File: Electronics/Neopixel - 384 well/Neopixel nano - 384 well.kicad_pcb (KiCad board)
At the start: 2 copper layers, 121.5 x 83 mm, 777 parts, among them J1 USB_B, J2 Conn_01x03_Male, U1 SAMD21_MOD

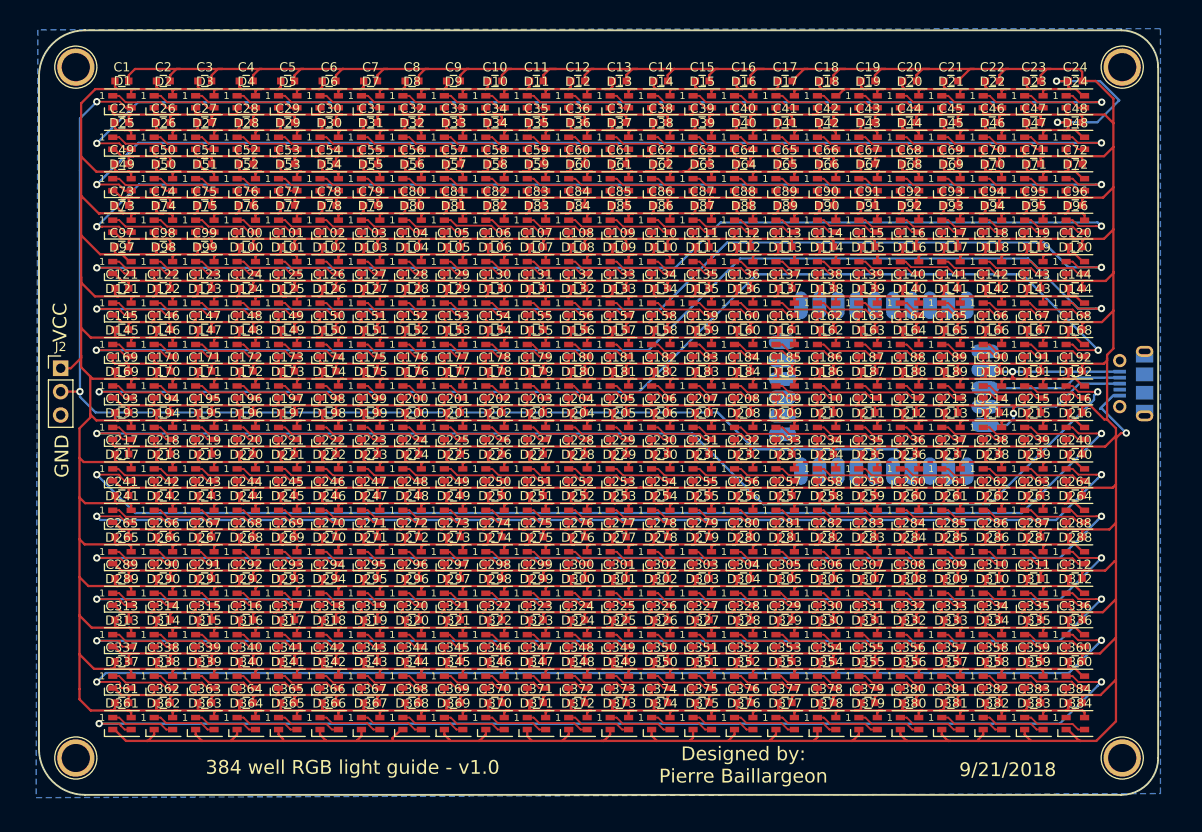
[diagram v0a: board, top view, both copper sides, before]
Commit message: Updated to v1.1
Updated to v1.1. Changes:
- Removed HCC module footprint from back to simplify design
- Added copper pour to front of PCB for +5V
- Added fiducuals for pick and place automation
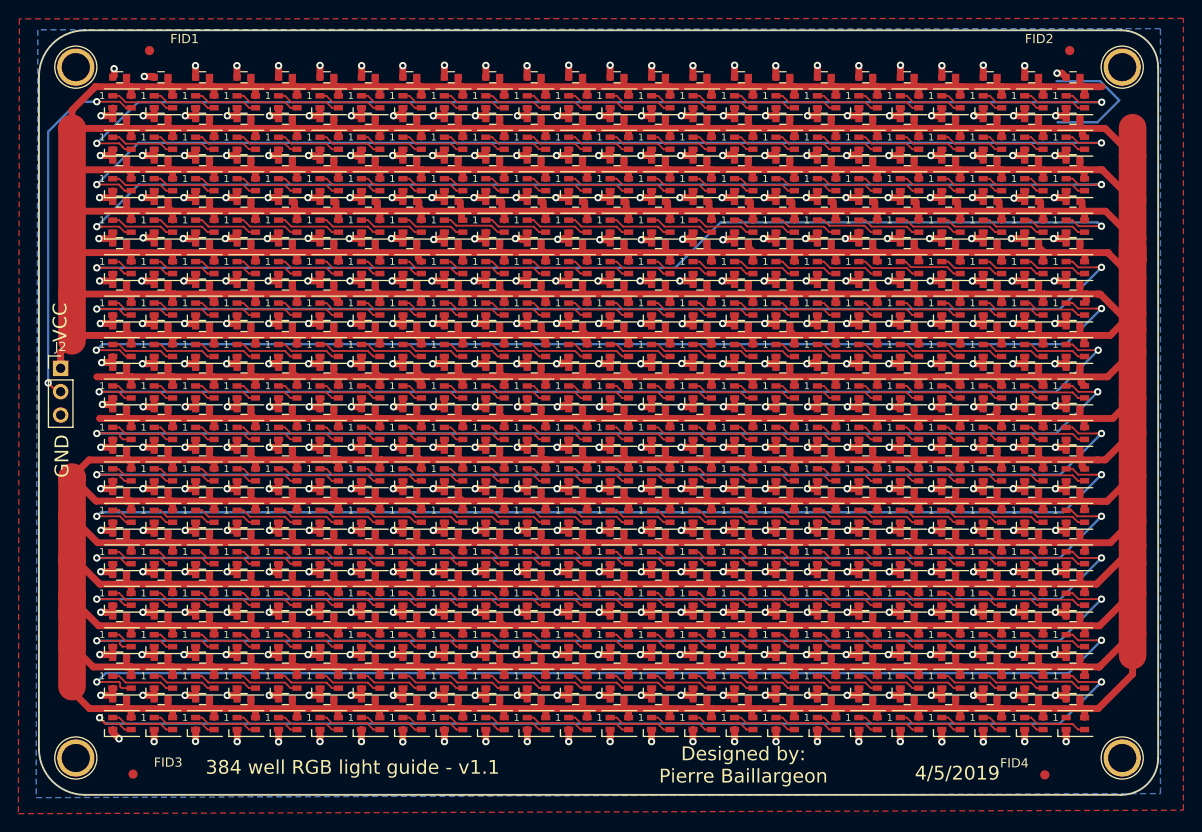
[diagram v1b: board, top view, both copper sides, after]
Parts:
- removed the G*** at (84.0, 110.0)
- removed J1: USB_B, Connectors_USB:USB_Micro-B_Molex-105017-0001
- removed U1: SAMD21_MOD, hcc mod:SAMD_HCC_G_FOOT
- added ?: , , F.Cu at (29.2, 38.6)
- added FID1: Fiducial_1mm_Mask3mm, Fiducials:Fiducial_1mm_Mask3mm, F.Cu at (52.0, 42.2)
- added FID2: Fiducial_1mm_Mask3mm, Fiducials:Fiducial_1mm_Mask3mm, F.Cu at (151.9, 42.2)
- added FID3: Fiducial_1mm_Mask3mm, Fiducials:Fiducial_1mm_Mask3mm, F.Cu at (50.2, 120.8)
- added FID4: Fiducial_1mm_Mask3mm, Fiducials:Fiducial_1mm_Mask3mm, F.Cu at (149.2, 120.8)
- added G***: MapleLogo, logos:MapleLogo, B.Cu at (77.5, 101.0)
- moved C139 0.47 mm to (129.8, 67.6), turned to 180 degrees
- moved C163 0.47 mm to (129.8, 72.1), turned to 180 degrees
- moved C187 0.47 mm to (129.8, 76.6), turned to 180 degrees
- moved C211 0.47 mm to (129.8, 81.1), turned to 180 degrees
- moved C235 0.47 mm to (129.8, 85.6), turned to 180 degrees
- moved C259 0.47 mm to (129.8, 90.1), turned to 180 degrees
- moved C283 0.47 mm to (129.8, 94.6), turned to 180 degrees
- moved C307 0.47 mm to (129.8, 99.1), turned to 180 degrees
- moved C331 0.47 mm to (129.8, 103.6), turned to 180 degrees
- moved C355 0.47 mm to (129.8, 108.1), turned to 180 degrees
- moved C379 0.47 mm to (129.8, 112.6), turned to 180 degrees
- moved C115 0.47 mm to (129.8, 63.1), turned to 180 degrees
- moved C19 0.47 mm to (129.8, 45.1), turned to 180 degrees
- moved C43 0.47 mm to (129.8, 49.6), turned to 180 degrees
- moved C67 0.47 mm to (129.8, 54.1), turned to 180 degrees
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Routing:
- net GND: track 2801.1 -> 925.4 mm, vias 2 -> 408
- net VCC: track 2675.4 -> 2788.7 mm, vias 3 -> 0
- net Net-(D1-Pad3): track 132.9 -> 39.7 mm
- net Net-(J1-Pad3): track 15.6 -> 0.00 mm
- net Net-(J1-Pad2): track 15.1 -> 0.00 mm
- net Net-(D168-Pad1): track 124.7 -> 117.8 mm
- net Net-(D192-Pad1): track 125.0 -> 118.4 mm
- net Net-(D144-Pad1): track 123.6 -> 119.1 mm
- net Net-(D216-Pad1): track 122.5 -> 119.6 mm
- net Net-(D120-Pad1): track 121.3 -> 119.1 mm
- added copper zone on F.Cu, net VCC
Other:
- board text added: "384 well RGB light guide - v1.1"
- board text added: "4/5/2019"
- board text removed: "384 well RGB light guide - v1.0"
- board text removed: "9/21/2018"
